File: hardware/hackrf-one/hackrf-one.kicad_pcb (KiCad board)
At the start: 4 copper layers, 120 x 75 mm, 432 parts, among them J1 USB-MICRO-B, J10 GND_CLIP, J2 RF-SHIELD-FRAME, J3 RF-SHIELD-COVER, J4 MOUNTING_HOLE, J5 MOUNTING_HOLE, J6 MOUNTING_HOLE, J7 MOUNTING_HOLE, J8 MOUNTING_HOLE, J9 MOUNTING_HOLE, P1 1V8, P13 GPO1, P14 XCVR_CLKOUT, P15 INTR, P16 CLKIN, P17 GPO6, P18 OEB, P19 GPO3, P2 CLKOUT, P20 GPIO, P21 REF_IN, P22 I2S, P23 DBGEN, P24 TRST, P25 LPC_ISP, P26 LPC_JTAG, P27 MIXER_SDATA, P28 SD, P29 CPLD_JTAG, P3 GND, P30 BANK2_AUX, P31 MIXER_SCLK, P32 MIXER_ENX, P33 MIXER_RESETX, P34 MIX_BYPASS, P35 !MIX_BYPASS, P36 VAA, P37 SCL, P38 SDA, P39 SSP1_SCK, P4 ANTENNA, P40 SSP1_MOSI, P41 SSP1_MISO, P42 TX, P43 RX, P44 HP, P45 LP, P46 TX_MIX_BP, P47 RX_MIX_BP, P48 TX_AMP, P49 RX_AMP, P5 LEDS, P50 AMP_BYPASS, P51 !TX_AMP_PWR, P52 !RX_AMP_PWR, P53 CS_XCVR, P54 CS_AD, P55 TXENABLE, P56 RXENABLE, P57 XTAL2, P58 GCK1, P59 GCK2, P6 GPO4, P60 SGPIO_CLK, P61 DA0, P62 DA7, P63 DD0, P64 DD9, P65 DA4, P66 DD5, P67 RSSI, P68 SPIFI_CS, P69 VREGMODE, P7 GPO2, P70 EN_1V8, P71 ID, P72 GP_CLKIN, P73 P1_2, P74 P1_1, P75 GP_CLKIN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

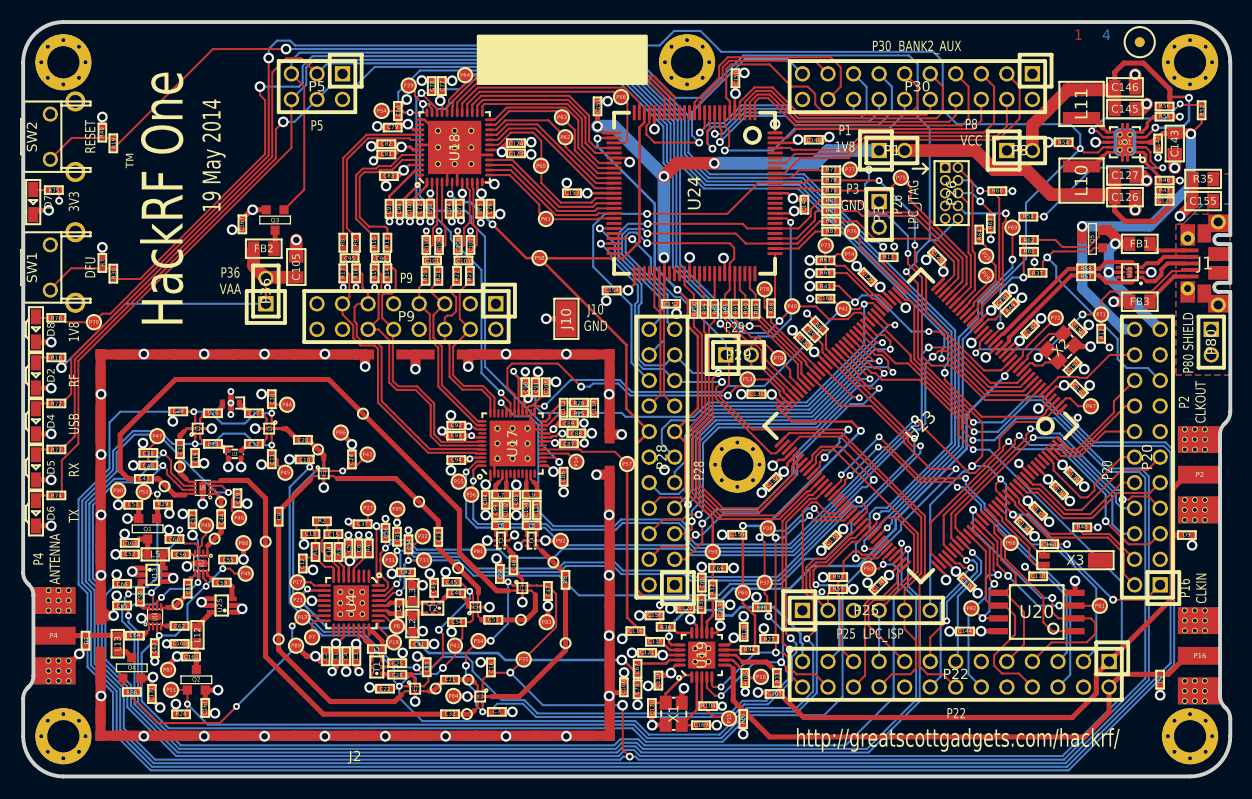
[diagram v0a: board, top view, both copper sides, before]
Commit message: Move RF section around to make room for protection (yet to be added)
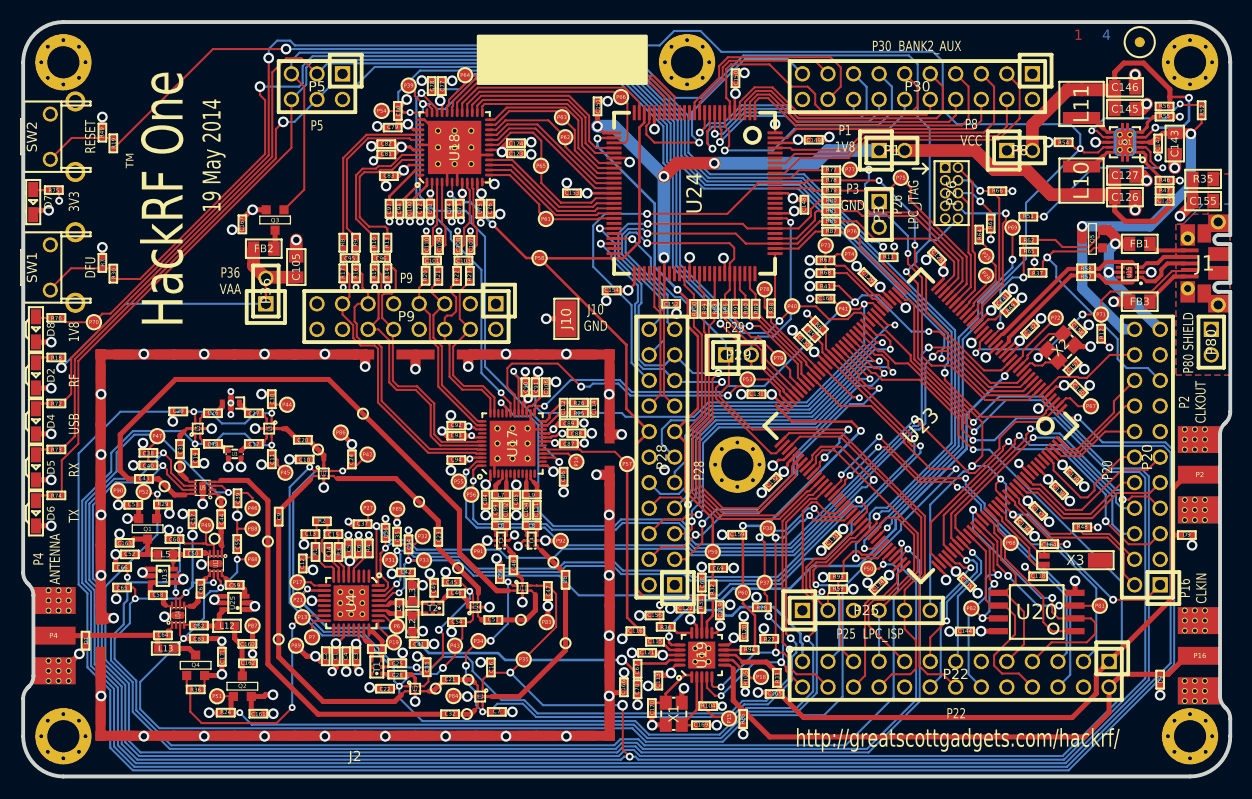
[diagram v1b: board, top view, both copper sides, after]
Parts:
- removed the TESTPOINT-30MIL-MASKONLY at (75.3, 157.8)
- moved P87 9.48 mm to (82.8, 160.0)
- moved C171 7.88 mm to (79.8, 163.1), turned to 90 degrees
- moved C160 6.75 mm to (82.3, 161.8), turned to 0 degrees
- moved Q4 6.36 mm to (77.2, 163.9)
- moved R36 6.36 mm to (77.2, 166.3)
- moved C162 5.69 mm to (82.3, 163.8), turned to 180 degrees
- moved C161 5.31 mm to (83.4, 168.8), turned to 0 degrees
- moved L13 4.79 mm to (74.2, 162.3), turned to 180 degrees
- moved P51 4.62 mm to (79.3, 167.0)
- moved Q2 4.62 mm to (81.8, 166.0)
- moved C63 4.48 mm to (77.5, 161.3), turned to 0 degrees
- moved R24 4.45 mm to (80.1, 168.7)
- moved L12 3.07 mm to (80.3, 160.0), turned to 180 degrees
- moved C64 2.79 mm to (73.9, 161.0)
- moved U14 2.29 mm to (75.4, 159.0)
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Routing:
- net RX_AMP: track 130.3 -> 136.7 mm
- net !TX_AMP_PWR: track 90.7 -> 85.2 mm
- net AMP_BYPASS: track 124.2 -> 129.0 mm
- net GND: track 592.3 -> 596.4 mm, vias 230 -> 226
- net Net-(C64-Pad2): track 7.51 -> 11.5 mm
- net VAA: track 92.7 -> 95.1 mm
- net RX_MIX_BP: track 192.3 -> 194.4 mm
- net /frontend/!ANT_BIAS: track 28.4 -> 26.7 mm
- net Net-(C160-Pad1): track 4.04 -> 5.51 mm
- net TX_AMP: track 143.2 -> 144.6 mm
- net Net-(C163-Pad2): track 4.17 -> 5.44 mm
- net LP: track 225.5 -> 226.5 mm
- net !MIX_BYPASS: track 237.4 -> 238.5 mm
- net Net-(C61-Pad1): track 3.22 -> 2.33 mm
- net TX_MIX_BP: track 215.0 -> 215.9 mm
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
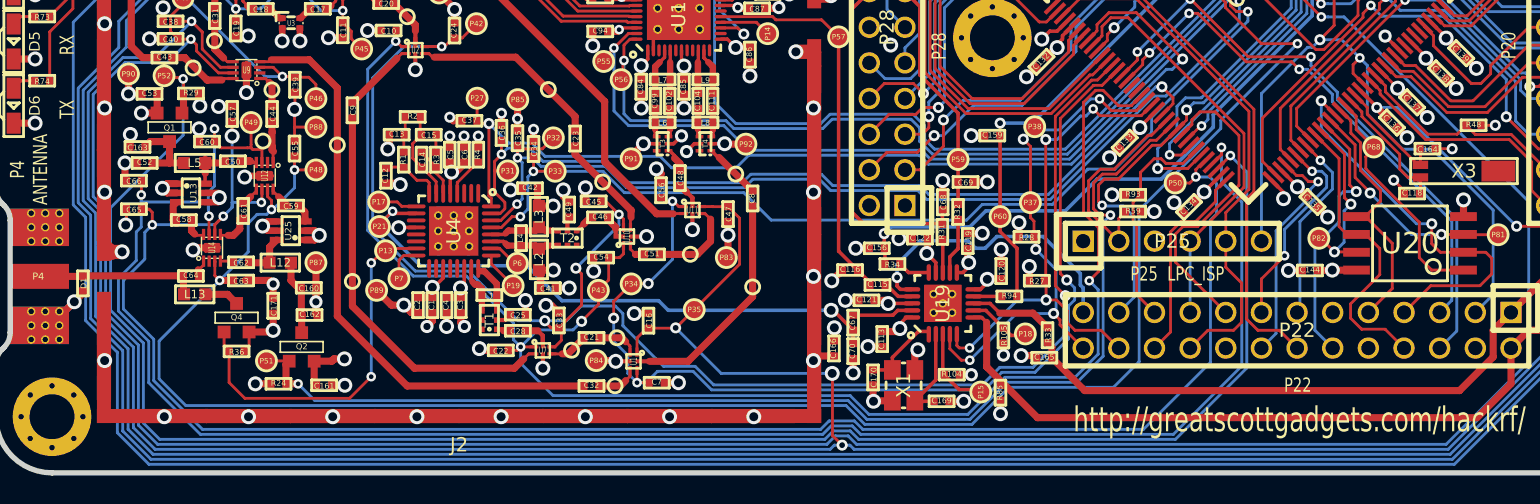
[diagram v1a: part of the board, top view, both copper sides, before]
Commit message: Corrected libraries (to use gsg-kicad-lib) and added SMP1330 protection
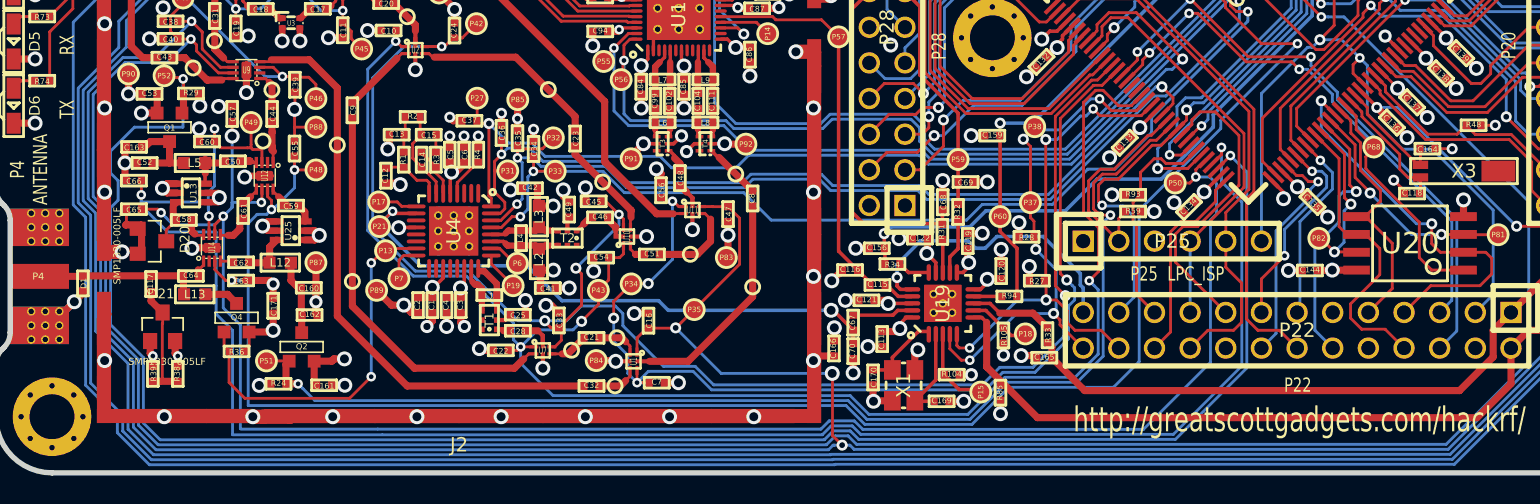
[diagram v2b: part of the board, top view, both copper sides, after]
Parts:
- added C117: 100nF, hackrf:GSG-0402, F.Cu at (71.1, 161.5)
- added D20: SMP1330-005LF, gsg-modules:SOT23-DD, F.Cu at (71.1, 158.5)
- added D21: SMP1330-005LF, gsg-modules:SOT23-DD, F.Cu at (71.9, 164.6)
- added R38: 10k, hackrf:GSG-0402, F.Cu at (73.0, 167.9)
- added R39: 10k, hackrf:GSG-0402, F.Cu at (71.2, 167.9)
- C169, C170: value DNP -> 1.8pF
- MARK1MM: footprint GSG-MARK1MM -> hackrf:GSG-MARK1MM
- TESTPOINT-30MIL-MASKONLY (x16): footprint GSG-TESTPOINT-30MIL-MASKONLY -> hackrf:GSG-TESTPOINT-30MIL-MASKONLY
- U15: value LXES1TBCC2-004 -> TVS
- moved C163 0.24 mm to (69.8, 151.8)
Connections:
- net /frontend/TX_AMP_OUT renamed Net-(C62-Pad1)
- net Net-(C58-Pad1) renamed /frontend/RX_AMP_IN
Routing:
- net Net-(C117-Pad2): track 0.00 -> 8.63 mm
- net TX_AMP: track 144.6 -> 137.7 mm
- net GND: track 596.4 -> 602.5 mm, vias 226 -> 225
- net AMP_BYPASS: track 129.0 -> 123.8 mm
- net !RX_AMP_PWR: track 130.3 -> 132.8 mm
- net Net-(C58-Pad2): track 1.72 -> 3.33 mm
- net VAA: track 95.1 -> 96.7 mm, vias 27 -> 28
- net RX_AMP: track 136.7 -> 136.1 mm

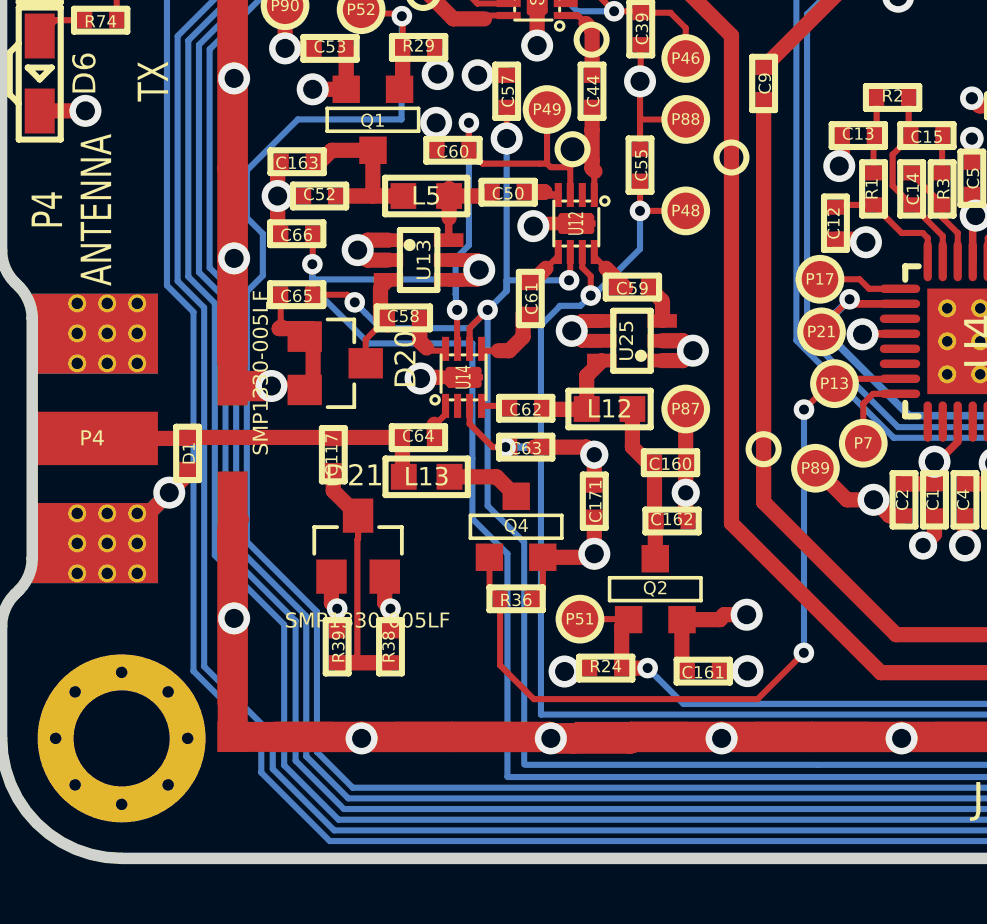
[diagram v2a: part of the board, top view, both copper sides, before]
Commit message: Improved RF layout by passing signals through protection devices instead of using stubs
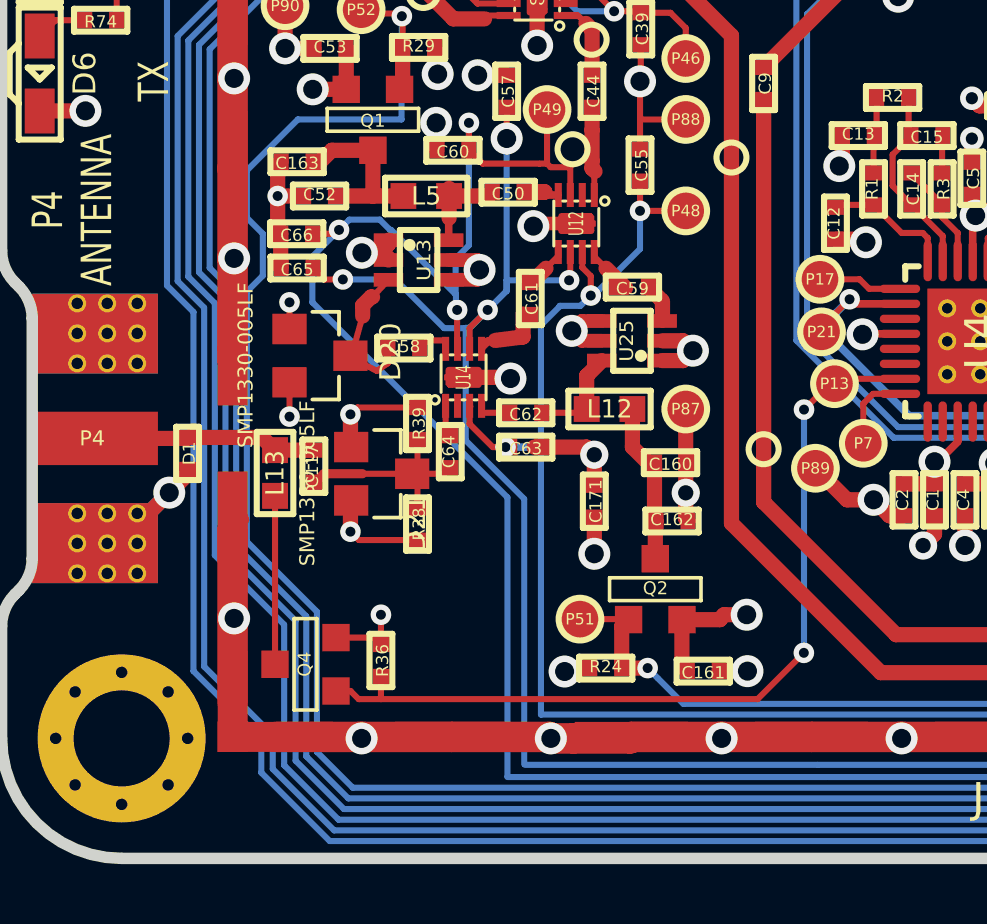
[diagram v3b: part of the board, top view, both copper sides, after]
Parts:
- moved Q4 8.38 mm to (70.1, 168.5), turned to 270 degrees
- moved R39 7.91 mm to (73.9, 160.5)
- moved L13 5.06 mm to (69.1, 162.2), turned to 90 degrees
- moved R36 4.95 mm to (72.6, 168.4), turned to 90 degrees
- moved R38 4.19 mm to (73.9, 163.9), turned to 90 degrees
- moved D21 2.54 mm to (72.7, 162.2), turned to 270 degrees
- moved C64 1.16 mm to (75.0, 161.4), turned to 270 degrees
- moved C58 1.00 mm to (73.4, 158.0)
- moved C65 0.89 mm to (69.8, 155.3)
- moved C117 0.75 mm to (70.4, 161.9)
- moved D20 0.57 mm to (70.6, 158.2)
- moved C62 0.15 mm to (77.5, 160.1)
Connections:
- C64 pad 2: Net-(C117-Pad1) -> Net-(C117-Pad2)
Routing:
- net Net-(C117-Pad1): track 11.5 -> 7.48 mm
- net Net-(L13-Pad1): track 2.49 -> 5.61 mm
- net GND: track 602.5 -> 600.3 mm, vias 225 -> 226
- net /frontend/!ANT_BIAS: track 26.7 -> 28.8 mm
- net RX_AMP: track 136.1 -> 134.5 mm
- net Net-(C58-Pad2): track 3.33 -> 4.76 mm
- net VAA: track 96.7 -> 98.0 mm, vias 28 -> 29
- net Net-(C117-Pad2): track 8.63 -> 7.40 mm
- net AMP_BYPASS: track 123.8 -> 124.6 mm
